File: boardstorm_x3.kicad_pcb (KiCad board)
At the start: 2 copper layers, 21 x 51 mm, 45 parts, among them J1 USB_C_Receptacle_USB2.0_14P, J2 Conn_01x20_Pin, J3 Conn_01x20_Pin, J4 Conn_01x03_Pin, J5 Conn_01x02, SW1 SW_Push, U2 MCP1700x-330xxTT, U3 W25Q16JVSS, U4 BQ24075RGT, U5 MAX17048G_T10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

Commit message: some more pcb updates
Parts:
- moved U2 87.7 mm to (110.3, 85.8), turned to 90 degrees
- moved U4 87.0 mm to (116.2, 86.9)
- moved J1 77.3 mm to (114.0, 77.8), turned to 180 degrees
- moved Y1 73.4 mm to (113.2, 108.1)
- moved U3 22.8 mm to (170.2, 101.5)
- moved J5 18.3 mm to (184.5, 101.0)
- moved SW1 11.3 mm to (206.1, 99.9)
- moved U5 5.48 mm to (206.5, 119.0)
- moved U1 4.51 mm to (114.0, 100.7)
- renumbered RP2040 to U1

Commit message: wow good progress shash
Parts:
- C1, C10, C11, C12, C15, C16, C17, C2, C20, C3, C4, C5, C6, C7, C8, C9: footprint Capacitor_SMD:C_0603_1608Metric -> Capacitor_SMD:C_0402_1005Metric
- C13, C14, C18, C19: footprint Capacitor_SMD:C_0805_2012Metric -> Capacitor_SMD:C_0603_1608Metric
- R1, R10, R11, R12, R13, R2, R3, R4, R5, R6, R7, R8, R9: footprint Resistor_SMD:R_0603_1608Metric -> Resistor_SMD:R_0402_1005Metric
- SW1: footprint Button_Switch_SMD:SW_SPST_TL3342 -> Button_Switch_SMD:SW_Push_SPST_NO_Alps_SKRK
- U3: value W25Q16JVSS -> W25Q16JVZPIQ TR; footprint Package_SO:SOIC-8_5.3x5.3mm_P1.27mm -> Package_SON:Winbond_USON-8-1EP_3x2mm_P0.5mm_EP0.2x1.6mm
- moved C14 83.1 mm to (126.0, 113.0)
- moved SW1 59.7 mm to (146.5, 96.2), turned to 180 degrees
- moved C13 57.3 mm to (145.2, 87.5), turned to 180 degrees
- moved C19 56.8 mm to (145.0, 93.1), turned to 180 degrees
- moved C15 53.8 mm to (145.5, 115.9), turned to -90 degrees
- moved R5 52.4 mm to (149.3, 113.4), turned to 180 degrees
- moved C10 52.1 mm to (152.0, 113.4), turned to -90 degrees
- moved C18 51.8 mm to (151.1, 94.4), turned to -45 degrees
- moved C3 50.8 mm to (143.3, 108.4), turned to 180 degrees
- moved R6 50.5 mm to (143.2, 96.9), turned to -90 degrees
- moved C2 50.1 mm to (151.0, 113.4), turned to -90 degrees
- moved R7 49.2 mm to (144.5, 98.8)
- moved C9 48.5 mm to (155.1, 109.0)
- moved R10 48.1 mm to (152.8, 96.2), turned to 90 degrees
- moved R3 47.9 mm to (150.7, 102.0), turned to 90 degrees
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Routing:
- net VBUS: track 0.00 -> 30.2 mm, vias 0 -> 3
- net GPIO0: track 0.00 -> 28.3 mm, vias 0 -> 1
- net GPIO29/ADC3: track 0.00 -> 27.2 mm
- net GPIO1: track 0.00 -> 26.5 mm, vias 0 -> 1
- net +3V3: track 0.00 -> 25.0 mm, vias 0 -> 2
- net GPIO3: track 0.00 -> 24.5 mm, vias 0 -> 1
- net GPIO15: track 0.00 -> 23.0 mm
- net GPIO2: track 0.00 -> 22.2 mm, vias 0 -> 1
- net GPIO28/ADC2: track 0.00 -> 21.7 mm
- net USB_D-: track 0.00 -> 21.0 mm
- net USB_D+: track 0.00 -> 21.0 mm
- net GPIO14: track 0.00 -> 19.6 mm
- net GPIO4: track 0.00 -> 17.4 mm
- net GPIO27/ADC1: track 0.00 -> 17.0 mm
- net GPIO26/ADC0: track 0.00 -> 15.6 mm, vias 0 -> 2
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
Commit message: pitstop
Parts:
- moved U5 81.6 mm to (151.7, 118.4), turned to -90 degrees
- moved J5 58.0 mm to (150.2, 124.1), turned to 180 degrees
- moved R12 42.8 mm to (147.3, 119.6), turned to -90 degrees
- moved R11 40.4 mm to (153.4, 97.8), turned to 180 degrees
- moved R13 39.7 mm to (148.9, 118.8)
- moved R9 37.5 mm to (153.3, 93.8), turned to 180 degrees
- moved C14 33.4 mm to (154.7, 95.9), turned to -90 degrees
- moved R8 1.49 mm to (154.9, 93.2)
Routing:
- net BAT+: track 4.48 -> 45.8 mm, vias 0 -> 3
- net GPIO4: track 17.4 -> 40.3 mm, vias 0 -> 2
- net GPIO16: track 0.00 -> 22.6 mm
- net SWDIO: track 0.00 -> 21.5 mm, vias 0 -> 1
- net SWCLK: track 0.00 -> 21.3 mm, vias 0 -> 1
- net GPIO5: track 15.3 -> 36.5 mm, vias 0 -> 2
- net GPIO17: track 0.00 -> 19.8 mm
- net RUN: track 0.00 -> 11.6 mm, vias 0 -> 1
- net Net-(U4-ILIM): track 0.00 -> 7.85 mm, vias 0 -> 2
- net (no net): track 5.13 -> 0.00 mm
- net GPIO3: track 24.5 -> 22.6 mm
- net GPIO24: track 11.6 -> 9.93 mm
- net Net-(U4-ISET): track 0.00 -> 1.51 mm
- net Net-(U4-TS): track 0.00 -> 1.30 mm
- net +3V3: track 25.0 -> 26.2 mm
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
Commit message: pcb update & more journals.. still fixing routes
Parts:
- U5: value MAX17048G_T10 -> MAX17048G+T10; footprint MAX17048G_T10:SON50P200X200X80-9N -> MAX17048G_T10:21-0168E_T822-3_MXM
- moved J5 2.27 mm to (148.2, 122.9), turned to 0 degrees
- moved R11 0.98 mm to (153.8, 98.8)
- moved R10 0.70 mm to (153.1, 96.8)
- moved C14 0.50 mm to (154.7, 96.4)
- moved C18 0.46 mm to (151.4, 94.7)
- moved C1 0.46 mm to (154.5, 102.0)
- moved U5 0.20 mm to (151.9, 118.4)
- moved C5 0.16 mm to (152.9, 102.7)
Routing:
- net SWDIO: track 21.5 -> 17.7 mm
- net SWCLK: track 21.3 -> 24.4 mm
- net VSYS: track 11.2 -> 13.9 mm
- net BAT+: track 45.8 -> 48.0 mm
- net Net-(U4-TMR): track 3.53 -> 4.98 mm
- net GND: track 8.91 -> 7.76 mm
- net GPIO10: track 7.66 -> 6.75 mm
- net VBUS: track 31.0 -> 30.2 mm
- net GPIO14: track 19.6 -> 20.3 mm
- net Net-(U4-ILIM): track 7.85 -> 8.60 mm
- net +3V3: track 26.2 -> 26.9 mm
- net GPIO26/ADC0: track 16.6 -> 15.9 mm
- net GPIO13: track 14.7 -> 15.2 mm

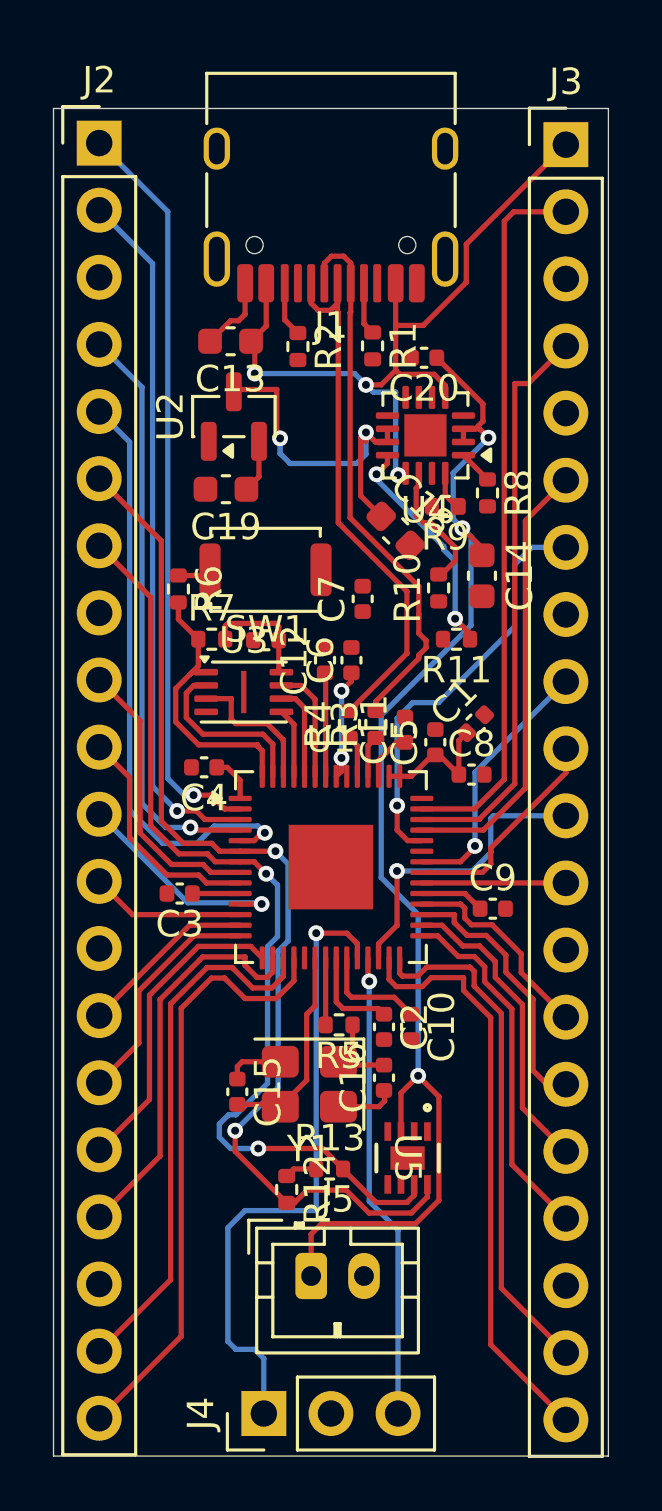
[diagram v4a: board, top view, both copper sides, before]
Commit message: added ESD protection IC, updated 3d models, fixed some wiring, added a power LED,
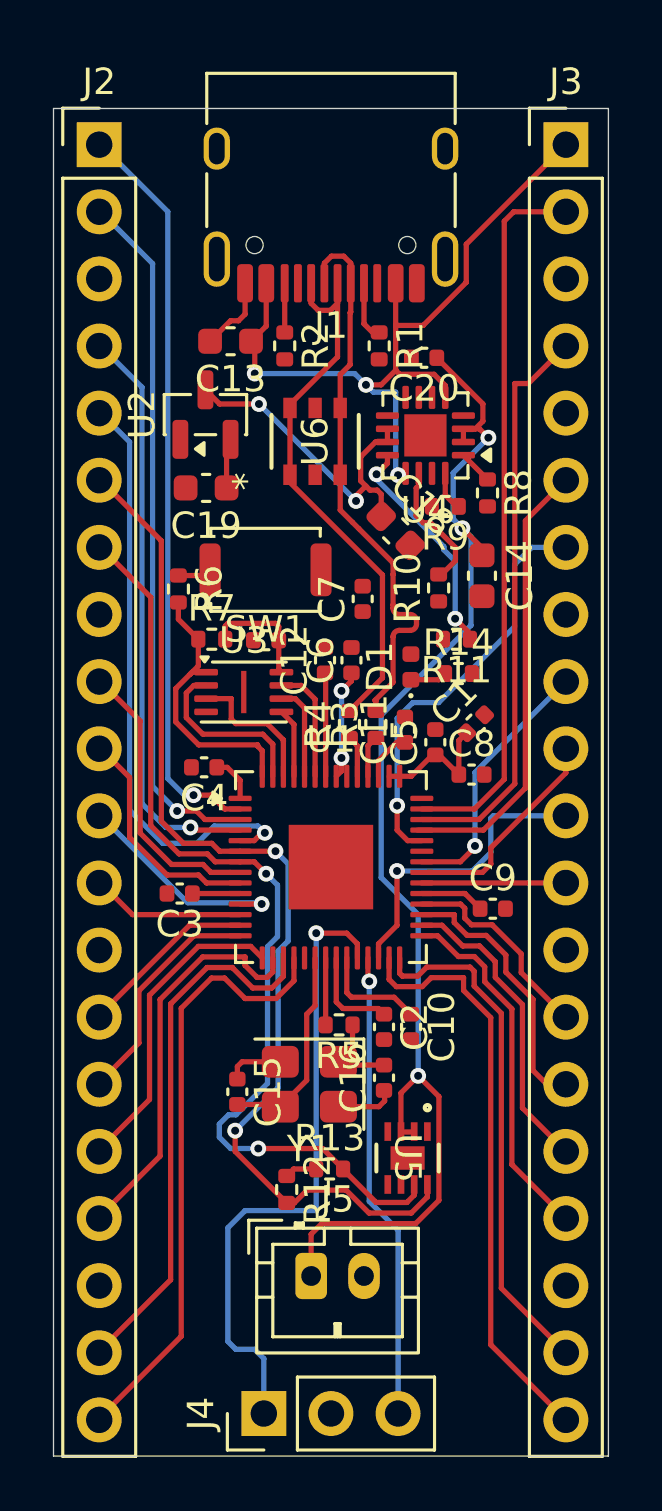
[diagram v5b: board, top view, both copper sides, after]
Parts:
- added D1: LED, LED_SMD:LED_0402_1005Metric, F.Cu at (152.0, 99.8)
- added R14: 4.7K, Resistor_SMD:R_0402_1005Metric, F.Cu at (153.8, 100.1)
- added U6: USBLC6-2SC6, USBLC6_2SC6:SOT23-6L_STM-L, F.Cu at (148.4, 91.3)
- U5: value MAX17048G+T10 -> MAX17048G_T10
- moved U2 1.08 mm to (144.2, 90.3)
- moved C19 0.75 mm to (144.3, 93.0)
- moved R2 0.50 mm to (147.2, 87.7)
- moved R1 0.25 mm to (150.8, 87.7)
- moved J2 0.06 mm to (140.2, 80.1)
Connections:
- U5 pad 2: unconnected-(U5-CELL-Pad2) -> BAT+
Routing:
- net Net-(D1-K): track 0.00 -> 1.39 mm
- net VSYS: track 13.9 -> 12.6 mm
- net USB_D+: track 21.0 -> 21.7 mm
- net USB_D-: track 21.0 -> 21.6 mm
- net BAT+: track 48.0 -> 48.5 mm

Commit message: i did someting but i forgot
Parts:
- C13: value 10uF -> 4.7uF
- J2, J3, J4: moved to B.Cu
- moved C10 0.63 mm to (152.4, 113.0), turned to 0 degrees
- moved C11 0.10 mm to (151.7, 102.2)
- turned J2 to 180 degrees
- turned J3 to 180 degrees
- turned J4 to -90 degrees
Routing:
- net +3V3: track 26.8 -> 119.2 mm, vias 2 -> 7
- net +1V1: track 9.88 -> 37.1 mm, vias 0 -> 2
- net RUN: track 11.6 -> 25.2 mm
- net VBUS: track 30.2 -> 33.8 mm, vias 3 -> 4
- net GPIO5: track 36.7 -> 39.2 mm
- net GPIO8: track 8.37 -> 9.38 mm
- net GPIO4: track 40.5 -> 41.2 mm
- net GPIO26/ADC0: track 15.9 -> 15.4 mm

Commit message: added images for the devboard
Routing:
- net GND: track 7.76 -> 108.9 mm, vias 0 -> 12
- added copper zone on B.Cu, net GND
- added copper zone on F.Cu, net GND

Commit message: fin
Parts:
- moved C20 1.18 mm to (153.7, 88.1)
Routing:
- net GND: track 108.9 -> 230.8 mm, vias 12 -> 37
- net GPIO0: track 28.3 -> 32.2 mm
- net GPIO3: track 23.0 -> 26.5 mm
- net GPIO1: track 26.5 -> 29.4 mm
- net GPIO2: track 22.2 -> 25.0 mm
- net GPIO4: track 41.2 -> 43.9 mm
- net VBUS: track 33.6 -> 35.0 mm
- net GPIO5: track 39.2 -> 40.5 mm
- net VSYS: track 12.6 -> 13.3 mm
- net SWDIO: track 17.7 -> 18.3 mm
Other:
- board text added: "BOARDSTORM-X3"
